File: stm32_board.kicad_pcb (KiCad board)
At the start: 2 copper layers, 28 parts, among them J1 USB_B_Micro, J2 Conn_01x04_Pin, J3 Conn_01x04_Pin, J4 Conn_01x04_Pin, SW1 SW_SPDT, U1 AMS1117-3.3, U2 STM32F103C8Tx, Y1 16MHz

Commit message: Updated PCB
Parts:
- SW1: footprint Button_Switch_THT:SW_E-Switch_EG1224_SPDT_Angled -> Button_Switch_SMD:SW_SPDT_PCM12
- moved R2 110.6 mm to (94.2, 39.5)
- moved J2 103.0 mm to (96.3, 34.2), turned to -90 degrees
- moved SW1 102.0 mm to (76.6, 34.6), turned to 180 degrees
- moved R4 100.0 mm to (94.8, 56.8), turned to 180 degrees
- moved R5 99.9 mm to (97.2, 56.8)
- moved C11 97.2 mm to (94.5, 54.8)
- moved J4 90.4 mm to (92.3, 59.8), turned to 90 degrees
- moved J3 5.01 mm to (108.8, 34.2)

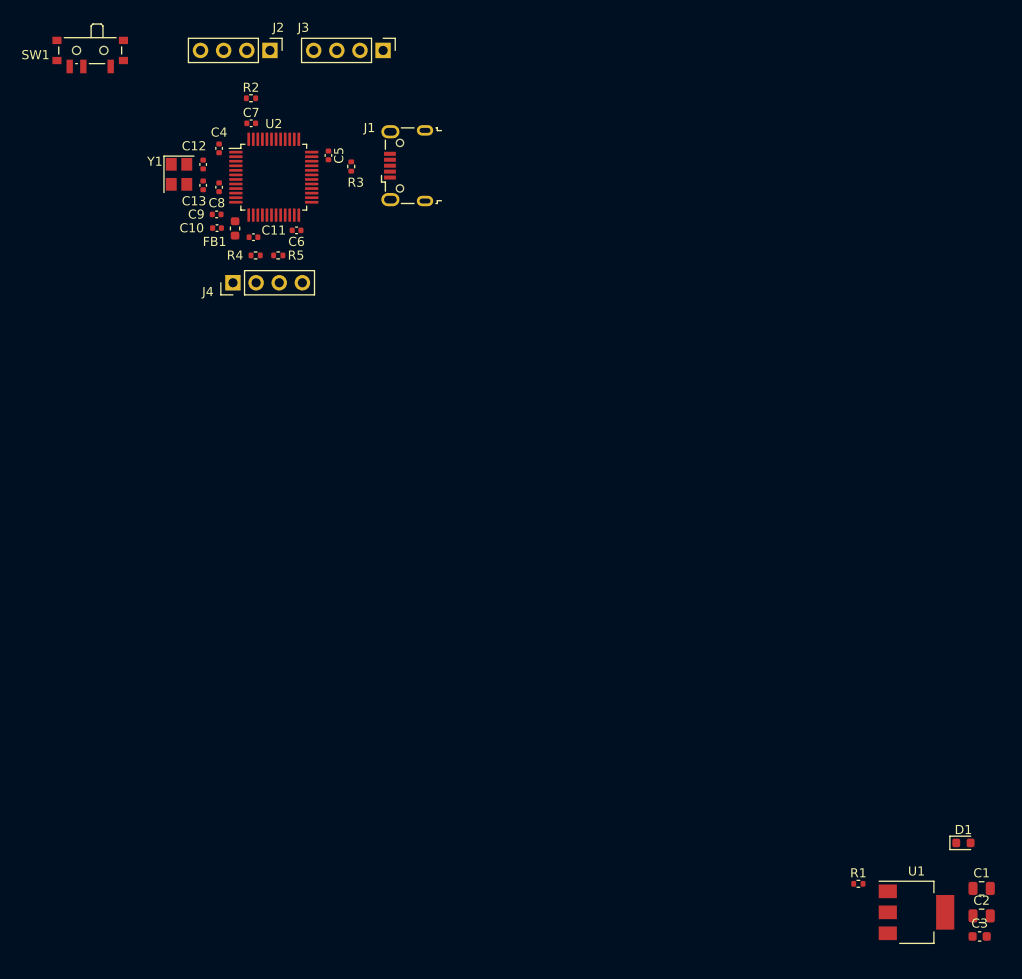
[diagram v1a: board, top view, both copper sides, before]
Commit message: Finished PCB routing
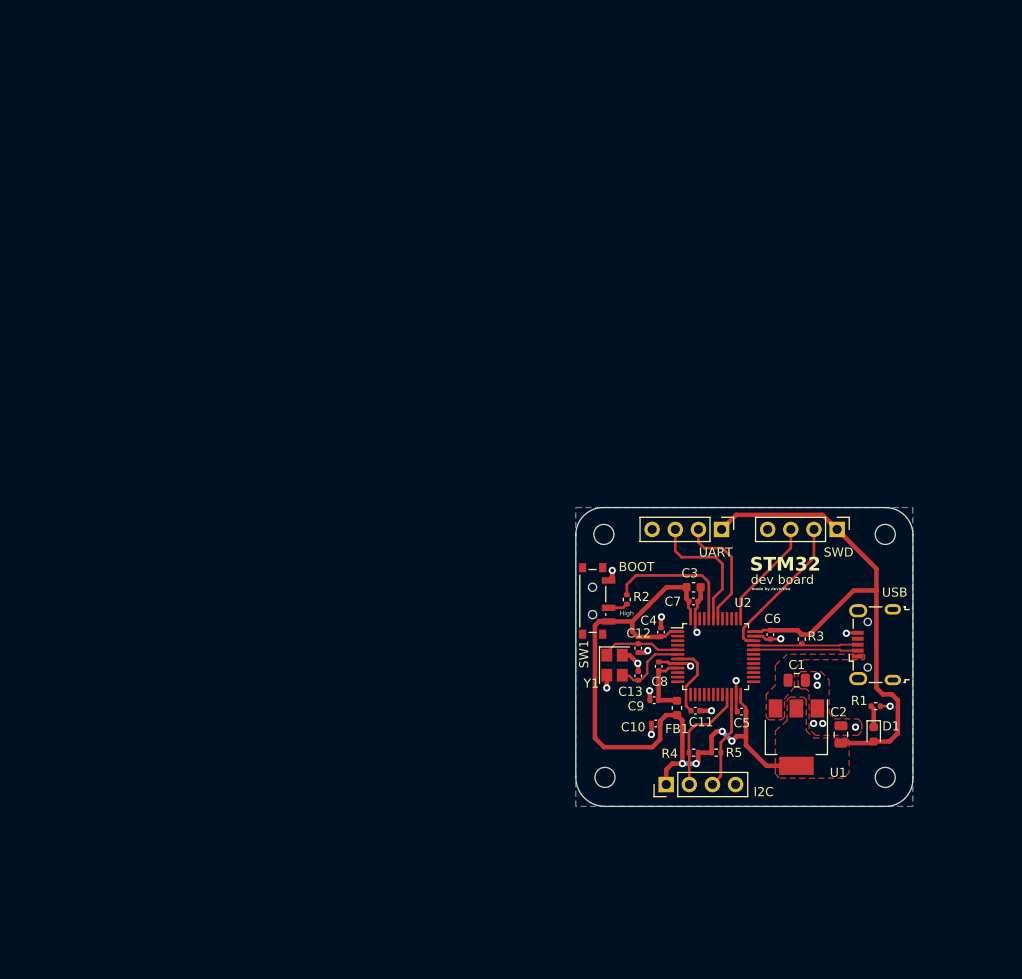
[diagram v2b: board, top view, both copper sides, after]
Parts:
- added H1: MountingHole, MountingHole:MountingHole_2.2mm_M2, F.Cu at (133.1, 114.0)
- added H2: MountingHole, MountingHole:MountingHole_2.2mm_M2, F.Cu at (163.9, 114.0)
- added H3: MountingHole, MountingHole:MountingHole_2.2mm_M2, F.Cu at (163.9, 87.4)
- added H4: MountingHole, MountingHole:MountingHole_2.2mm_M2, F.Cu at (133.0, 87.4)
- moved SW1 81.8 mm to (132.1, 94.7), turned to -90 degrees
- moved C5 76.1 mm to (148.1, 106.8), turned to 180 degrees
- moved J1 73.5 mm to (162.7, 99.5)
- moved J4 72.8 mm to (139.8, 114.8)
- moved R4 72.7 mm to (142.8, 111.3)
- moved R5 72.7 mm to (145.3, 111.3)
- moved C10 72.6 mm to (138.7, 108.1), turned to 180 degrees
- moved J3 72.4 mm to (158.6, 86.8)
- moved J2 72.3 mm to (145.9, 86.8)
- moved Y1 72.0 mm to (134.2, 101.7)
- moved C13 72.0 mm to (136.8, 102.9)
- moved C4 71.9 mm to (139.2, 98.1)
- moved C9 71.8 mm to (138.5, 105.6)
- moved R3 71.7 mm to (154.7, 98.9)
- moved FB1 71.6 mm to (141.0, 106.4)
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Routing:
- net +3.3V: track 0.00 -> 141.0 mm, vias 0 -> 4
- net GND: track 0.00 -> 29.6 mm, vias 0 -> 19
- net /SWDIO: track 0.00 -> 16.4 mm
- net /BOOT0: track 0.00 -> 14.9 mm
- net /USART1_RX: track 0.00 -> 14.6 mm
- net /USART1_TX: track 0.00 -> 13.1 mm
- net /I2C2_SCL: track 0.00 -> 12.4 mm
- net /SWCLK: track 0.00 -> 12.1 mm
- net /USB_D-: track 0.00 -> 11.6 mm
- net /USB_D+: track 0.00 -> 11.5 mm
- net /I2C2_SDA: track 0.00 -> 10.8 mm
- net /HSE_IN: track 0.00 -> 8.76 mm
- net /NRST: track 0.00 -> 8.31 mm
- net /HSE_OUT: track 0.00 -> 8.22 mm
- net +3.3VA: track 0.00 -> 7.52 mm
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- added copper zone on F.Cu, net +3.3V
- added copper zone on B.Cu, net GND
- added copper zone on F.Cu, net GND
- added copper zone on F.Cu, net VBUS
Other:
- board outline added: 37 x 32.8 mm
- board text added: "BOOT"
- board text added: "High"
- board text added: "I2C"
- board text added: "STM32"
- board text added: "SWD"
- board text added: "UART"
- board text added: "USB"
- board text added: "dev board"
- board text added: "made by devnithw"
